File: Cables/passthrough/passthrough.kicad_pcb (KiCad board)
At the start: 2 copper layers, 40 x 18.5 mm, 32 parts, among them J1 DB25_Male, J10 Conn_01x01, J11 Conn_01x01, J12 Conn_01x01, J13 Conn_01x01, J14 Conn_01x01, J15 Conn_01x01, J16 Conn_01x01, J17 Conn_01x01, J18 Conn_01x01, J19 Conn_01x01, J2 Conn_01x01, J20 Conn_01x01, J21 Conn_01x01, J22 Conn_01x01, J23 Conn_01x01, J24 Conn_01x01, J25 Conn_01x01, J26 Conn_01x01, J27 Conn_01x01, J28 Conn_01x01, J29 Conn_01x01, J3 Conn_01x01, J30 Conn_01x01, J31 Conn_01x01, J4 Conn_01x01, J5 Conn_01x01, J6 Conn_01x01, J7 Conn_01x01, J8 Conn_01x01, J9 Conn_01x01

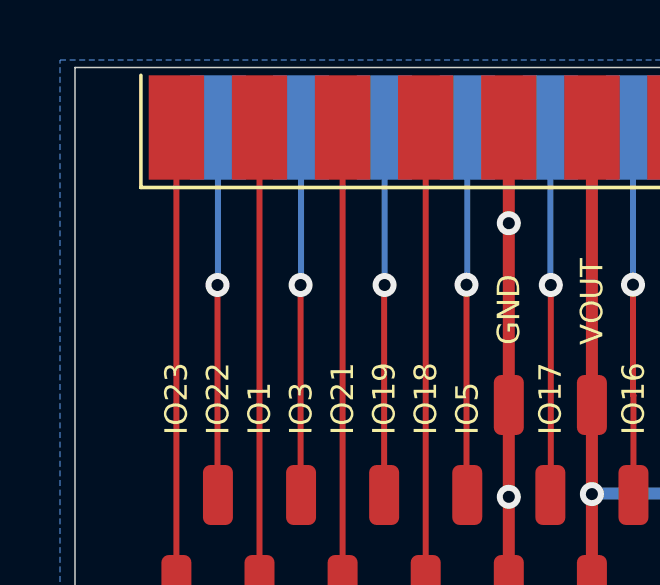
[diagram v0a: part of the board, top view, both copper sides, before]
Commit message: [PT] Add silkscreen info
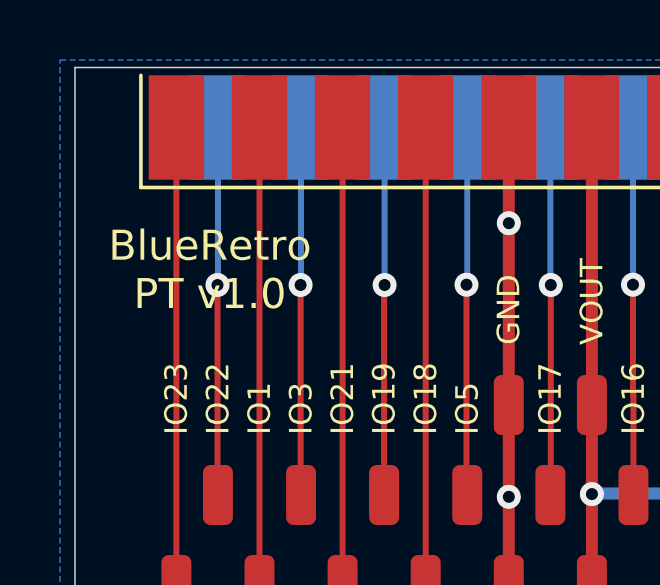
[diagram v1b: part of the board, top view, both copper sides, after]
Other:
- board text added: "BlueRetro PT v1.0"
- board text added: "© 2020 Jacques Gagnon Licensed under CERN-OHL-P-2.0 https://hackaday.io/project/170365-blueretro https://github.com/darthcloud/BlueRetro"

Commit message: Tweak PT & LS PCBs
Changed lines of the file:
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@@
   )
   (page A4)
+  (title_block
+    (title "BlueRetro Passthrough cable adapter")
+    (date 2020-09-05)
+    (rev v1.0)
+  )
   (layers
     (0 F.Cu signal)
@@
     (effects (font (size 1 1) (thickness 0.15)) (justify left mirror))
   )
-  (gr_text "BlueRetro\nPT v1.0" (at -15.5 -2.5) (layer F.SilkS)
-    (effects (font (size 1 1) (thickness 0.15)))
+  (gr_text "BlueRetro\nPT v1.0" (at -19.5 -2.5) (layer F.SilkS)
+    (effects (font (size 1 1) (thickness 0.15)) (justify left))
   )
   (gr_text LO (at 4.99 -4.12) (layer F.SilkS)

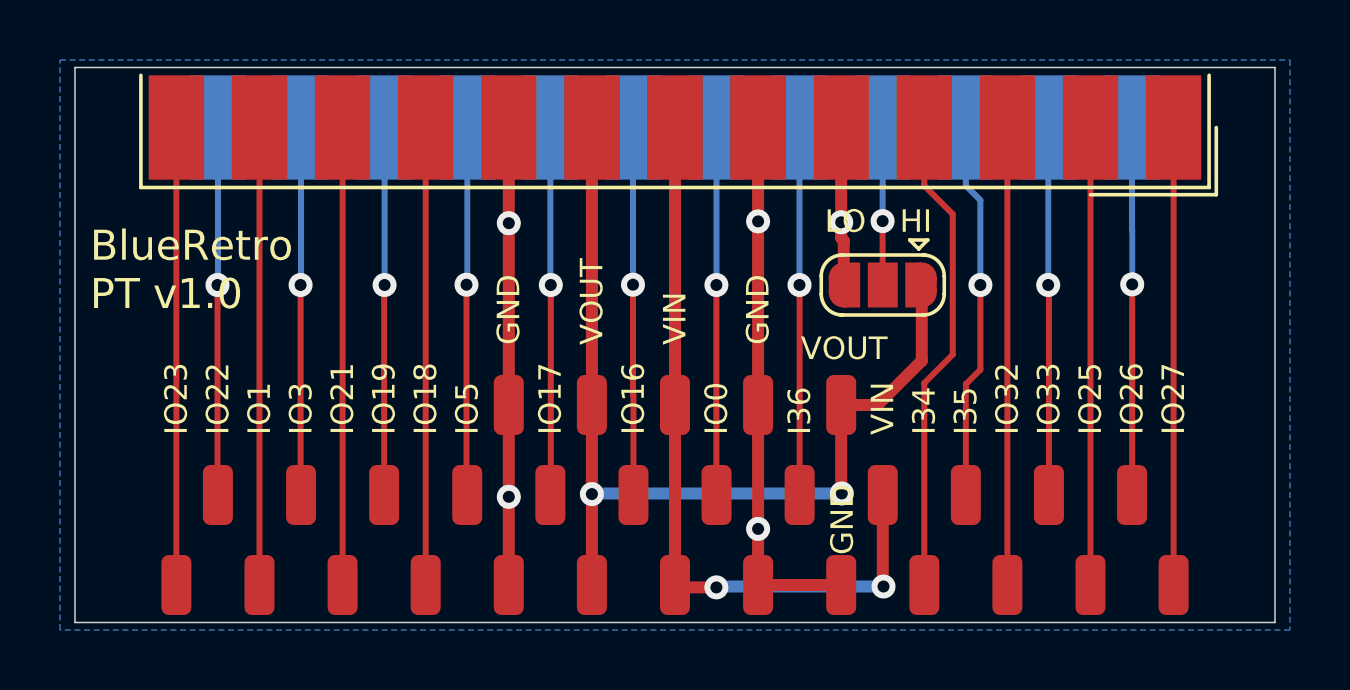
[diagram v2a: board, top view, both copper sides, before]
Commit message: Fix reversed DB25 on PT PCB
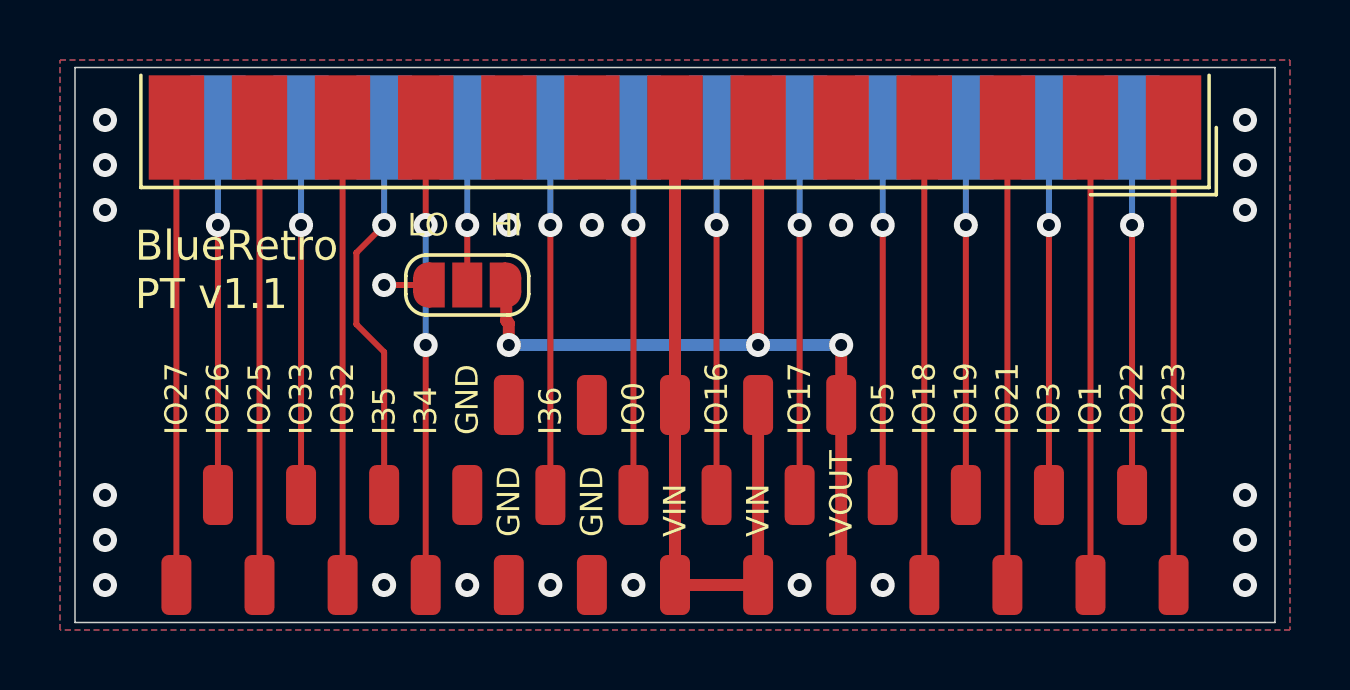
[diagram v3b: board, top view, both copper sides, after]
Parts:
- moved J28 33.2 mm to (-16.6, 8.00)
- moved J5 33.2 mm to (16.6, 8.00)
- moved J27 30.5 mm to (-15.2, 5.00)
- moved J6 30.5 mm to (15.2, 5.00)
- moved J26 27.7 mm to (-13.8, 8.00)
- moved J7 27.7 mm to (13.8, 8.00)
- moved J25 24.9 mm to (-12.5, 5.00)
- moved J8 24.9 mm to (12.5, 5.00)
- moved J24 22.2 mm to (-11.1, 8.00)
- moved J9 22.2 mm to (11.1, 8.00)
- moved J10 19.4 mm to (9.70, 5.00)
- moved J23 19.4 mm to (-9.70, 5.00)
- moved J11 16.6 mm to (8.31, 8.00)
- moved J22 16.6 mm to (-8.31, 8.00)
- moved J12 13.8 mm to (6.92, 5.00)
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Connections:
- J1 pad 1: /IO27 -> /IO23
- J1 pad 10: /IO18 -> /I34
- J1 pad 11: /IO21 -> /IO32
- J1 pad 12: /IO1 -> /IO25
- J1 pad 13: /IO23 -> /IO27
- J1 pad 14: /IO26 -> /IO22
- J1 pad 15: /IO33 -> /IO3
- J1 pad 16: /I35 -> /IO19
- J1 pad 17: /I39 -> /IO5
- J1 pad 18: /I36 -> /IO17
- J1 pad 19: /IO0 -> /IO16
- J1 pad 2: /IO25 -> /IO1
- J1 pad 20: /IO16 -> /IO0
- J1 pad 21: /IO17 -> /I36
- J1 pad 22: /IO5 -> /I39
- J1 pad 23: /IO19 -> /I35
- J1 pad 24: /IO3 -> /IO33
- J1 pad 25: /IO22 -> /IO26
- J1 pad 3: /IO32 -> /IO21
- J1 pad 4: /I34 -> /IO18
- J1 pad 6: /GND -> /VOUT
- J1 pad 8: /VOUT -> /GND
- J4 pad 1: /VOUT -> /VIN
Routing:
- net /GND: track 38.6 -> 1.47 mm, vias 5 -> 22
- net /VOUT: track 32.4 -> 28.4 mm, vias 2 -> 3
- net /VIN: track 25.3 -> 24.0 mm, vias 2 -> 0
- net /I34: track 16.0 -> 15.2 mm, vias 0 -> 2
- added copper zone on F.Cu, net /GND
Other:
- board text added: "BlueRetro PT v1.1"
- board text removed: "BlueRetro PT v1.0"

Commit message: Add LDO for PlayStation
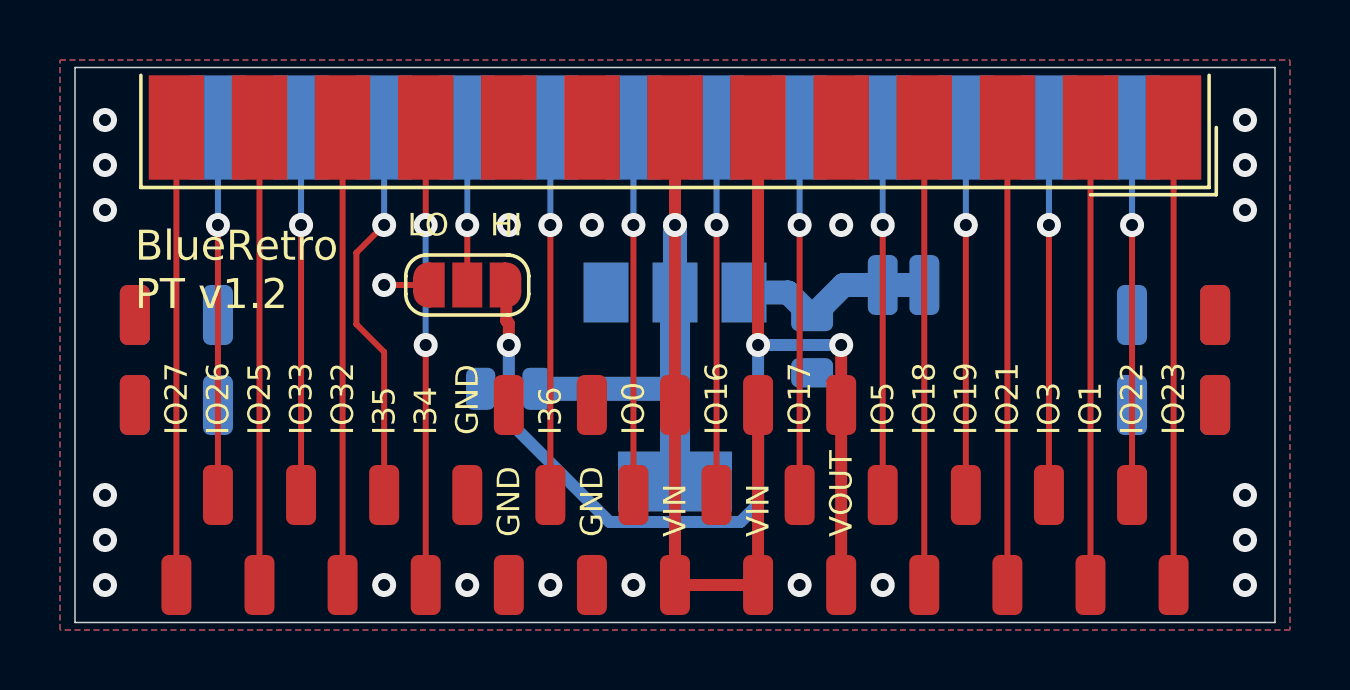
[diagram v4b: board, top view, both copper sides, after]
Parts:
- added C1: 10u, passthrough:C_0805_2012Metric, B.Cu at (4.57, -0.01)
- added C2: 10u, passthrough:C_0805_2012Metric, B.Cu at (-5.54, 1.46)
- added J32: Conn_01x01, passthrough:SolderWirePad_1x01_SMD_1x2mm, B.Cu at (8.31, -2.00)
- added J33: Conn_01x01, passthrough:SolderWirePad_1x01_SMD_1x2mm, B.Cu at (6.92, -2.00)
- added J34: Conn_01x01, passthrough:SolderWirePad_1x01_SMD_1x2mm, F.Cu at (18.0, -1.00)
- added J35: Conn_01x01, passthrough:SolderWirePad_1x01_SMD_1x2mm, F.Cu at (18.0, 2.00)
- added J36: Conn_01x01, passthrough:SolderWirePad_1x01_SMD_1x2mm, F.Cu at (-18.0, -1.00)
- added J37: Conn_01x01, passthrough:SolderWirePad_1x01_SMD_1x2mm, F.Cu at (-18.0, 2.00)
- added J38: Conn_01x01, passthrough:SolderWirePad_1x01_SMD_1x2mm, B.Cu at (18.0, 2.00)
- added J39: Conn_01x01, passthrough:SolderWirePad_1x01_SMD_1x2mm, B.Cu at (18.0, -1.00)
- added J40: Conn_01x01, passthrough:SolderWirePad_1x01_SMD_1x2mm, B.Cu at (-18.0, 2.00)
- added J41: Conn_01x01, passthrough:SolderWirePad_1x01_SMD_1x2mm, B.Cu at (-18.0, -1.00)
- added J42: Conn_01x01, passthrough:SolderWirePad_1x01_SMD_1x2mm, B.Cu at (15.2, 2.00)
- added J43: Conn_01x01, passthrough:SolderWirePad_1x01_SMD_1x2mm, B.Cu at (15.2, -1.00)
- added J44: Conn_01x01, passthrough:SolderWirePad_1x01_SMD_1x2mm, B.Cu at (-15.2, -1.00)
- added J45: Conn_01x01, passthrough:SolderWirePad_1x01_SMD_1x2mm, B.Cu at (-15.2, 2.00)
- added U1: AZ1117-3.3, passthrough:SOT-223-3_TabPin2, B.Cu at (0.00, 1.40)
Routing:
- net /VIN: track 24.0 -> 37.3 mm, vias 0 -> 1
- net /VOUT: track 28.4 -> 37.9 mm
- net Net-(C1-Pad1): track 0.00 -> 6.78 mm
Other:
- board text added: "BlueRetro PT v1.2"
- board text added: "VALT"
- board text added: "https://hackaday.io/project/170365-blueretro https://github.com/darthcloud/BlueRetro"
- board text added: "© 2020 Jacques Gagnon Licensed under CERN-OHL-P-2.0"
- board text removed: "BlueRetro PT v1.1"
- board text removed: "© 2020 Jacques Gagnon Licensed under CERN-OHL-P-2.0 https://hackaday.io/project/170365-blueretro https://github.com/darthcloud/BlueRetro"

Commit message: Generate cable schematic PDF & add license info
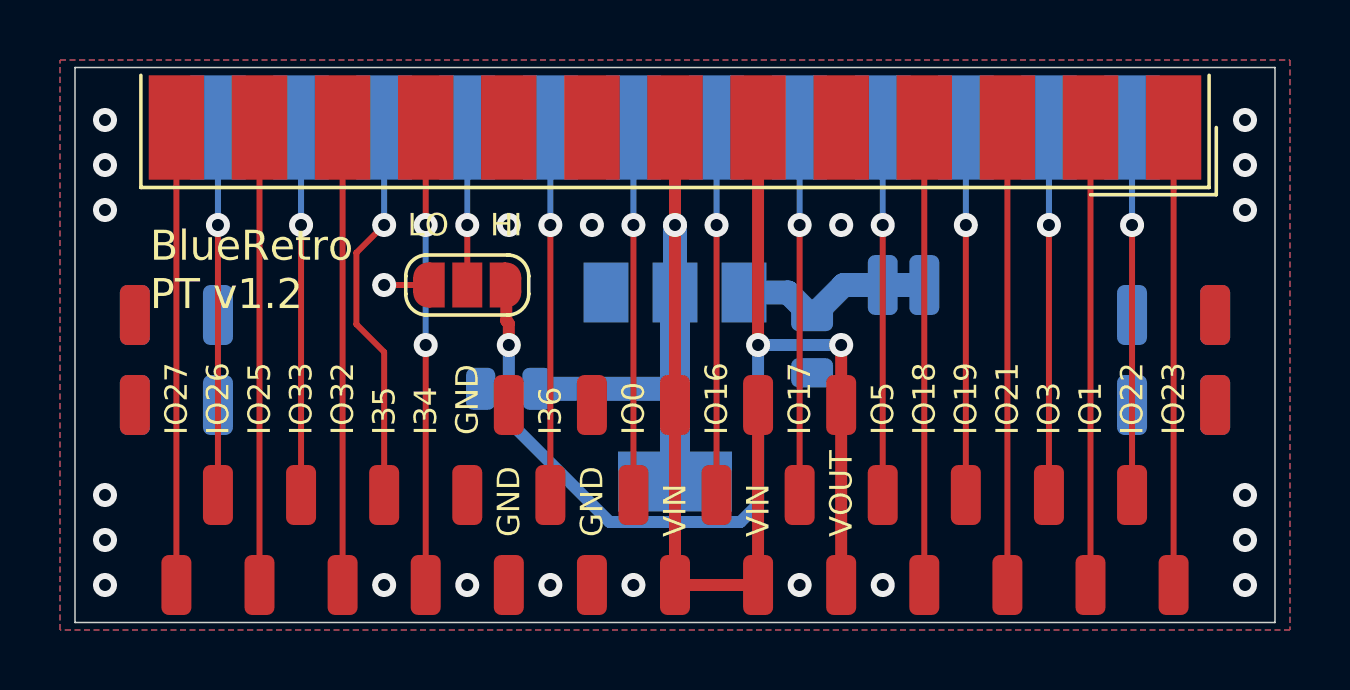
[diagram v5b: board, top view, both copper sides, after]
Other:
- board text added: "Licensed under CERN-OHL-P-2.0"
- board text added: "© 2020 Jacques Gagnon"
- board text removed: "© 2020 Jacques Gagnon Licensed under CERN-OHL-P-2.0"
